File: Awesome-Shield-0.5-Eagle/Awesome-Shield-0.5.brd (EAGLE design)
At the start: 100 x 80 mm, 24 parts, among them J1 ARDUINO_R3_SHIELDUNO_R3_SHIEL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, SW1 SPST_TACT-EVQQ2

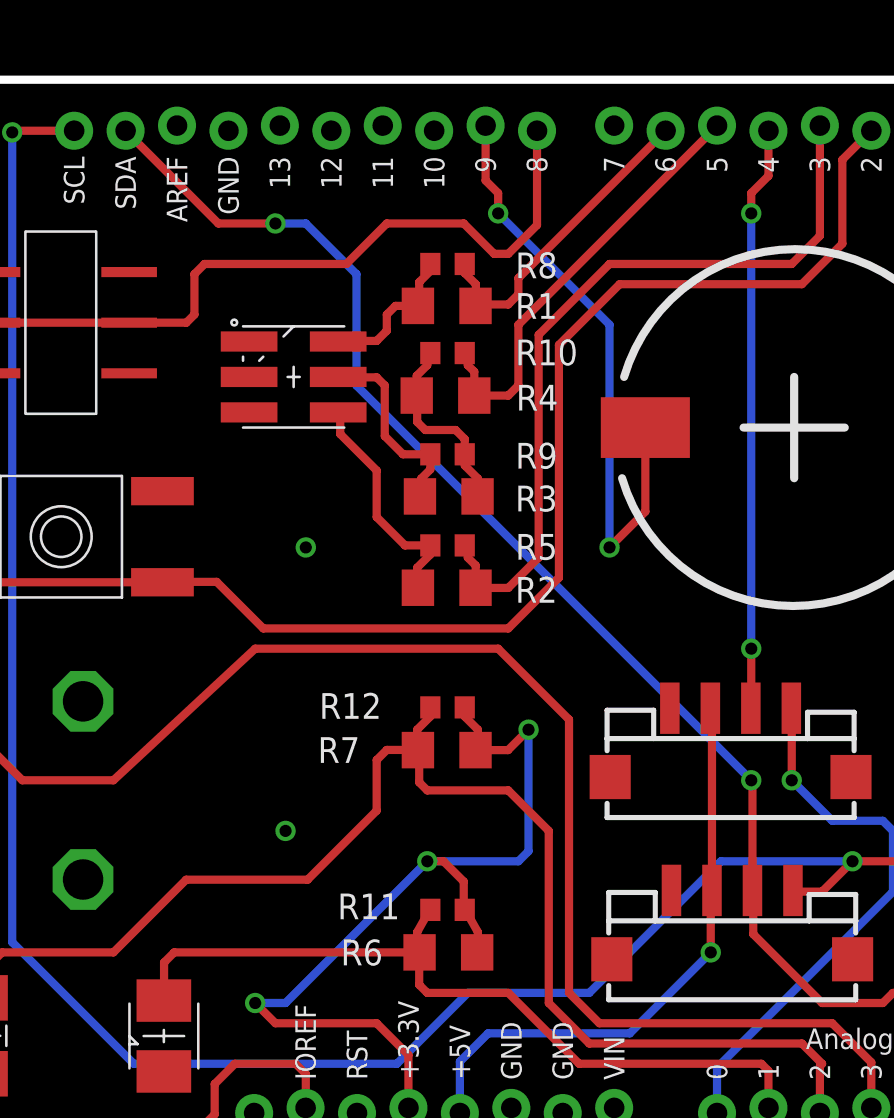
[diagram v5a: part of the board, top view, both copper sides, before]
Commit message: removed redundant vias, trace tweaks
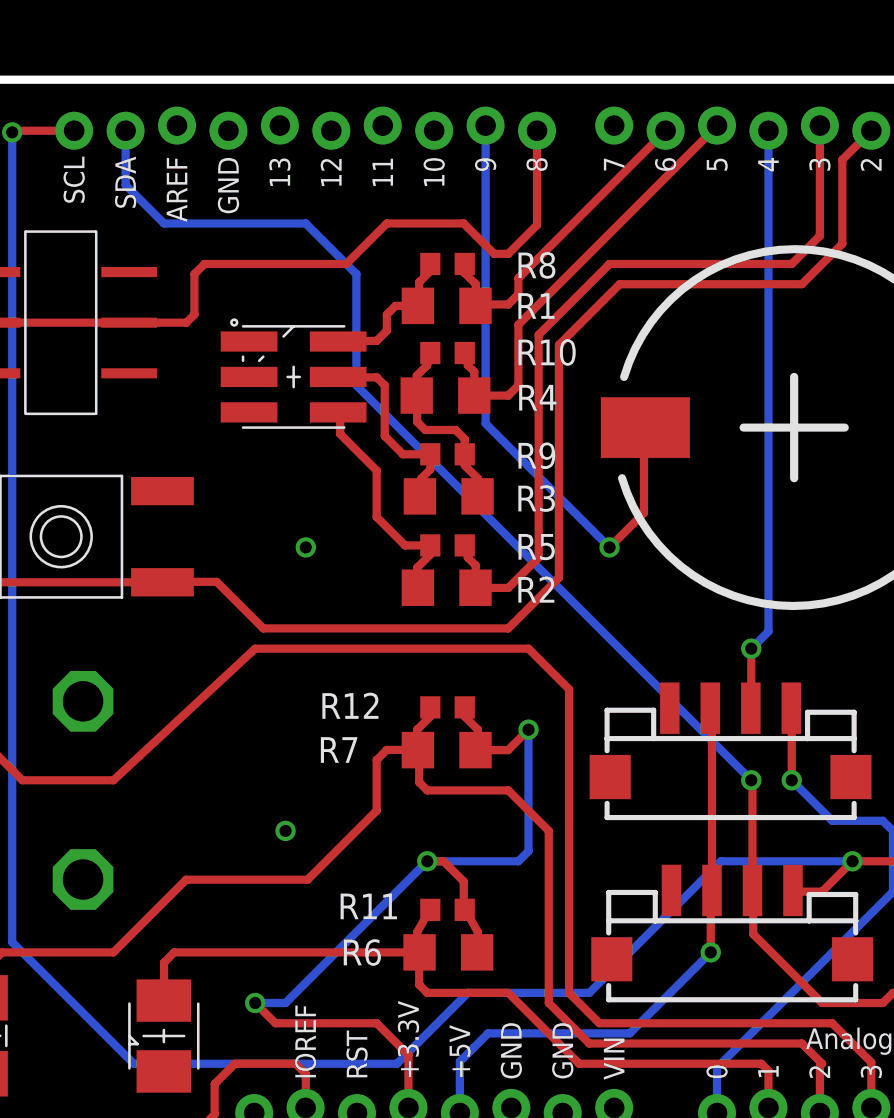
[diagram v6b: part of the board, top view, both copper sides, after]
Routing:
- net SDA: track 65.1 -> 66.6 mm, vias 2 -> 1
- net A3: track 67.9 -> 68.8 mm
- net D9: vias 2 -> 1
- net D4: vias 2 -> 1
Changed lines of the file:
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@@
 <contactref element="J5" pad="1"/>
 <contactref element="SJ2" pad="1"/>
-<wire x1="35.56" y1="68.58" x2="32.58" y2="68.58" width="0.4064" layer="1"/>
 <wire x1="32.58" y1="68.58" x2="32.5" y2="68.5" width="0.4064" layer="1"/>
 <via x="32.5" y="68.5" extent="1-16" drill="0.6"/>
@@
 <wire x1="51.5" y1="22.5" x2="55" y2="26" width="0.4064" layer="16"/>
 <wire x1="55" y1="26" x2="61" y2="26" width="0.4064" layer="16"/>
+<wire x1="35.56" y1="68.58" x2="32.58" y2="68.58" width="0.4064" layer="1"/>
 </signal>
 <signal name="SDA">
@@
 <wire x1="69" y1="36.5" x2="49.5" y2="56" width="0.4064" layer="16"/>
 <wire x1="49.5" y1="56" x2="49.5" y2="61.5" width="0.4064" layer="16"/>
-<via x="45.5" y="64" extent="1-16" drill="0.6"/>
-<wire x1="45.5" y1="64" x2="42.68" y2="64" width="0.4064" layer="1"/>
-<wire x1="42.68" y1="64" x2="38.1" y2="68.58" width="0.4064" layer="1"/>
 <wire x1="72.5" y1="25.5" x2="75.5" y2="25.5" width="0.4064" layer="1"/>
 <wire x1="75.5" y1="25.5" x2="76" y2="26" width="0.4064" layer="1"/>
@@
 <wire x1="77.492" y1="26" x2="77.5" y2="26.008" width="0.4064" layer="1"/>
 <wire x1="49.5" y1="61.5" x2="47" y2="64" width="0.4064" layer="16"/>
-<wire x1="47" y1="64" x2="45.5" y2="64" width="0.4064" layer="16"/>
+<wire x1="38.1" y1="68.58" x2="38.1" y2="65.9" width="0.4064" layer="16"/>
+<wire x1="38.1" y1="65.9" x2="40" y2="64" width="0.4064" layer="16"/>
+<wire x1="40" y1="64" x2="47" y2="64" width="0.4064" layer="16"/>
 </signal>
 <signal name="D8">
@@
 <contactref element="J1" pad="D9"/>
 <contactref element="SG1" pad="-"/>
-<wire x1="63.77" y1="53.92" x2="63.77" y2="49.77" width="0.4064" layer="1"/>
-<wire x1="63.77" y1="49.77" x2="62" y2="48" width="0.4064" layer="1"/>
+<wire x1="55.88" y1="68.834" x2="55.88" y2="54.12" width="0.4064" layer="16"/>
+<wire x1="55.88" y1="54.12" x2="62" y2="48" width="0.4064" layer="16"/>
 <via x="62" y="48" extent="1-16" drill="0.6"/>
-<wire x1="62" y1="48" x2="62" y2="59" width="0.4064" layer="16"/>
-<wire x1="62" y1="59" x2="56.5" y2="64.5" width="0.4064" layer="16"/>
-<via x="56.5" y="64.5" extent="1-16" drill="0.6"/>
-<wire x1="56.5" y1="64.5" x2="56.5" y2="65.5" width="0.4064" layer="1"/>
-<wire x1="55.88" y1="68.834" x2="55.88" y2="66.12" width="0.4064" layer="1"/>
-<wire x1="55.88" y1="66.12" x2="56.5" y2="65.5" width="0.4064" layer="1"/>
+<wire x1="62" y1="48" x2="63.7" y2="49.7" width="0.4064" layer="1"/>
+<wire x1="63.7" y1="49.7" x2="63.7" y2="53.85" width="0.4064" layer="1"/>
+<wire x1="63.7" y1="53.85" x2="63.77" y2="53.92" width="0.4064" layer="1"/>
 </signal>
 <signal name="D4">
 <contactref element="J1" pad="D4"/>
 <contactref element="J2" pad="2"/>
-<wire x1="69.85" y1="68.58" x2="69.85" y2="66.35" width="0.4064" layer="1"/>
-<via x="69" y="64.5" extent="1-16" drill="0.6"/>
-<wire x1="69" y1="64.5" x2="69" y2="43" width="0.4064" layer="16"/>
 <via x="69" y="43" extent="1-16" drill="0.6"/>
 <wire x1="69" y1="43" x2="69" y2="40.08" width="0.4064" layer="1"/>
 <wire x1="69" y1="40.08" x2="68.98" y2="40.06" width="0.4064" layer="1"/>
-<wire x1="69.85" y1="66.35" x2="69" y2="65.5" width="0.4064" layer="1"/>
-<wire x1="69" y1="65.5" x2="69" y2="64.5" width="0.4064" layer="1"/>
+<wire x1="69.85" y1="68.58" x2="69.85" y2="43.85" width="0.4064" layer="16"/>
+<wire x1="69.85" y1="43.85" x2="69" y2="43" width="0.4064" layer="16"/>
 </signal>
 <signal name="N$2">
@@
 <wire x1="74.93" y1="22.57" x2="73" y2="24.5" width="0.4064" layer="1"/>
 <wire x1="73" y1="24.5" x2="61.5" y2="24.5" width="0.4064" layer="1"/>
-<wire x1="60" y1="39.5" x2="56.5" y2="43" width="0.4064" layer="1"/>
-<wire x1="56.5" y1="43" x2="44.5" y2="43" width="0.4064" layer="1"/>
+<wire x1="58" y1="43" x2="44.5" y2="43" width="0.4064" layer="1"/>
 <wire x1="44.5" y1="43" x2="37.5" y2="36.5" width="0.4064" layer="1"/>
 <wire x1="37.5" y1="36.5" x2="33" y2="36.5" width="0.4064" layer="1"/>
@@
 <wire x1="31" y1="38.5" x2="29" y2="38.5" width="0.4064" layer="1"/>
 <wire x1="61.5" y1="24.5" x2="60" y2="26" width="0.4064" layer="1"/>
-<wire x1="60" y1="26" x2="60" y2="39.5" width="0.4064" layer="1"/>
+<wire x1="60" y1="26" x2="60" y2="41" width="0.4064" layer="1"/>
+<wire x1="58" y1="43" x2="60" y2="41" width="0.4064" layer="1"/>
 </signal>
 <signal name="IOREF">

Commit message: removed redundant via, trace nudges for GND pour coverage
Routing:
- net D3: track 38.4 -> 36.4 mm
- net SCL: track 103.5 -> 101.8 mm, vias 2 -> 1
- net D2: track 65.3 -> 64.2 mm
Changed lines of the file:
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@@
 <via x="46" y="34" extent="1-16" drill="0.6"/>
 <via x="81" y="45.5" extent="1-16" drill="0.6"/>
+<via x="30" y="66" extent="1-16" drill="0.6"/>
 <wire x1="74.006" y1="27.66" x2="73.926" y2="36.66" width="0" layer="19" extent="1-1"/>
 </signal>
@@
 <wire x1="57" y1="44" x2="59.5" y2="46.5" width="0.4064" layer="1"/>
 <wire x1="59.5" y1="46.5" x2="59.5" y2="58" width="0.4064" layer="1"/>
-<wire x1="59.5" y1="58" x2="62.5" y2="61" width="0.4064" layer="1"/>
-<wire x1="62.5" y1="61" x2="71.5" y2="61" width="0.4064" layer="1"/>
-<wire x1="71.5" y1="61" x2="73.5" y2="63" width="0.4064" layer="1"/>
-<wire x1="73.5" y1="63" x2="73.5" y2="67.15" width="0.4064" layer="1"/>
-<wire x1="73.5" y1="67.15" x2="74.93" y2="68.58" width="0.4064" layer="1"/>
 <wire x1="44.9" y1="44" x2="42.6" y2="46.3" width="0.4064" layer="1"/>
 <wire x1="42.6" y1="46.3" x2="39.94" y2="46.3" width="0.4064" layer="1"/>
 <wire x1="39.94" y1="46.3" x2="39.92" y2="46.28" width="0.4064" layer="1"/>
+<wire x1="59.5" y1="58" x2="67" y2="65.5" width="0.4064" layer="1"/>
+<wire x1="67" y1="65.5" x2="74" y2="65.5" width="0.4064" layer="1"/>
+<wire x1="74" y1="65.5" x2="75" y2="66.5" width="0.4064" layer="1"/>
+<wire x1="75" y1="66.5" x2="75" y2="68.51" width="0.4064" layer="1"/>
+<wire x1="75" y1="68.51" x2="74.93" y2="68.58" width="0.4064" layer="1"/>
 </signal>
 <signal name="D6">
@@
 <contactref element="J5" pad="1"/>
 <contactref element="SJ2" pad="1"/>
-<wire x1="32.58" y1="68.58" x2="32.5" y2="68.5" width="0.4064" layer="1"/>
-<via x="32.5" y="68.5" extent="1-16" drill="0.6"/>
-<wire x1="32.5" y1="68.5" x2="32.5" y2="28.5" width="0.4064" layer="16"/>
 <via x="74" y="32.5" extent="1-16" drill="0.6"/>
 <wire x1="71" y1="31.12" x2="71.06" y2="31.06" width="0.4064" layer="1"/>
@@
 <wire x1="71.12" y1="31" x2="71.06" y2="31.06" width="0.4064" layer="1"/>
 <wire x1="67.5" y1="32.5" x2="61" y2="26" width="0.4064" layer="16"/>
-<wire x1="38.5" y1="22.5" x2="32.5" y2="28.5" width="0.4064" layer="16"/>
+<wire x1="38.5" y1="22.5" x2="33" y2="28" width="0.4064" layer="16"/>
 <wire x1="74" y1="32.5" x2="67.5" y2="32.5" width="0.4064" layer="16"/>
 <wire x1="38.5" y1="22.5" x2="51.5" y2="22.5" width="0.4064" layer="16"/>
 <wire x1="51.5" y1="22.5" x2="55" y2="26" width="0.4064" layer="16"/>
 <wire x1="55" y1="26" x2="61" y2="26" width="0.4064" layer="16"/>
-<wire x1="35.56" y1="68.58" x2="32.58" y2="68.58" width="0.4064" layer="1"/>
+<wire x1="35.56" y1="68.58" x2="35.56" y2="68.56" width="0.4064" layer="16"/>
+<wire x1="35.56" y1="68.56" x2="32.5" y2="65.5" width="0.4064" layer="16"/>
+<wire x1="32.5" y1="65.5" x2="32.5" y2="28.5" width="0.4064" layer="16"/>
+<wire x1="32.5" y1="28.5" x2="33" y2="28" width="0.4064" layer="16"/>
 </signal>
 <signal name="SDA">
@@
 <contactref element="R5" pad="1"/>
 <contactref element="R2" pad="1"/>
-<wire x1="72.39" y1="68.834" x2="72.39" y2="63.39" width="0.4064" layer="1"/>
 <wire x1="55.392" y1="46" x2="55.392" y2="47.108" width="0.4064" layer="1"/>
 <wire x1="55.392" y1="47.108" x2="55" y2="47.5" width="0.4064" layer="1"/>
 <wire x1="55" y1="47.5" x2="55" y2="47.85" width="0.4064" layer="1"/>
 <wire x1="55" y1="47.85" x2="54.85" y2="48.1" width="0.4064" layer="1"/>
-<wire x1="72.39" y1="63.39" x2="71" y2="62" width="0.4064" layer="1"/>
-<wire x1="71" y1="62" x2="62" y2="62" width="0.4064" layer="1"/>
-<wire x1="62" y1="62" x2="58.5" y2="58.5" width="0.4064" layer="1"/>
 <wire x1="58.5" y1="58.5" x2="58.5" y2="47.5" width="0.4064" layer="1"/>
 <wire x1="58.5" y1="47.5" x2="57" y2="46" width="0.4064" layer="1"/>
 <wire x1="57" y1="46" x2="55.392" y2="46" width="0.4064" layer="1"/>
 <wire x1="55.392" y1="46" x2="55.382" y2="46.01" width="0.4064" layer="1"/>
+<wire x1="58.5" y1="58.5" x2="66.5" y2="66.5" width="0.4064" layer="1"/>
+<wire x1="66.5" y1="66.5" x2="72" y2="66.5" width="0.4064" layer="1"/>
+<wire x1="72" y1="66.5" x2="72.5" y2="67" width="0.4064" layer="1"/>
+<wire x1="72.5" y1="67" x2="72.5" y2="68.724" width="0.4064" layer="1"/>
+<wire x1="72.5" y1="68.724" x2="72.39" y2="68.834" width="0.4064" layer="1"/>
 </signal>
 <signal name="N$9">

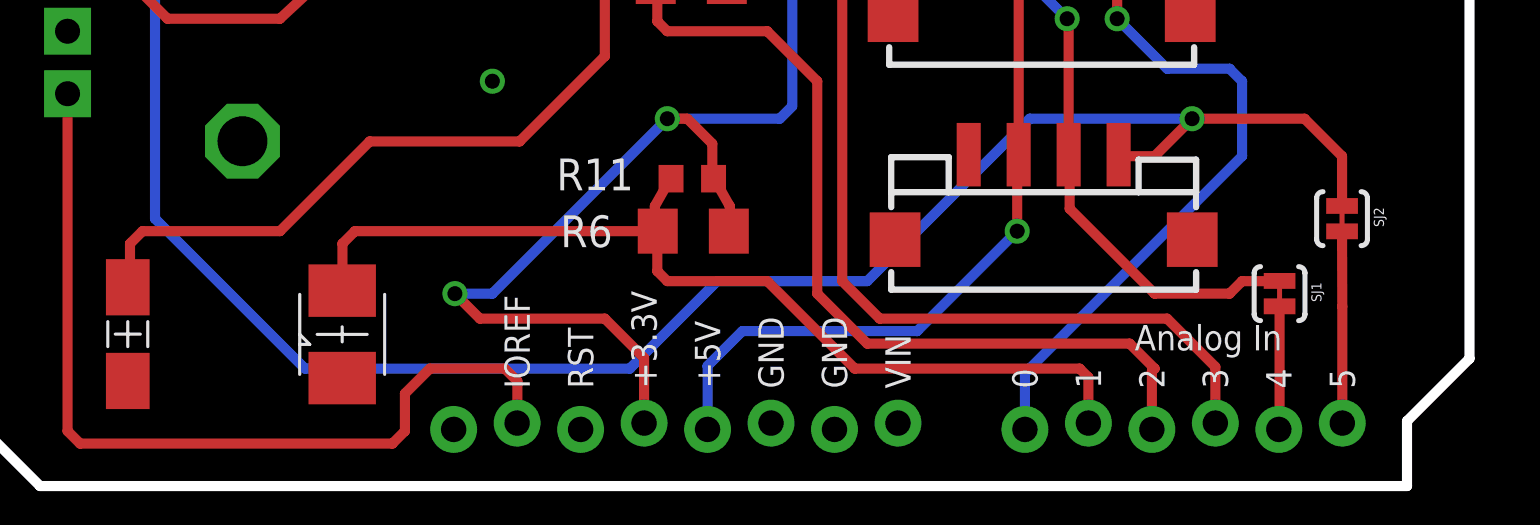
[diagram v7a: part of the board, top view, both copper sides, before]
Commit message: alligned solder bridge pads to make cutting them easier
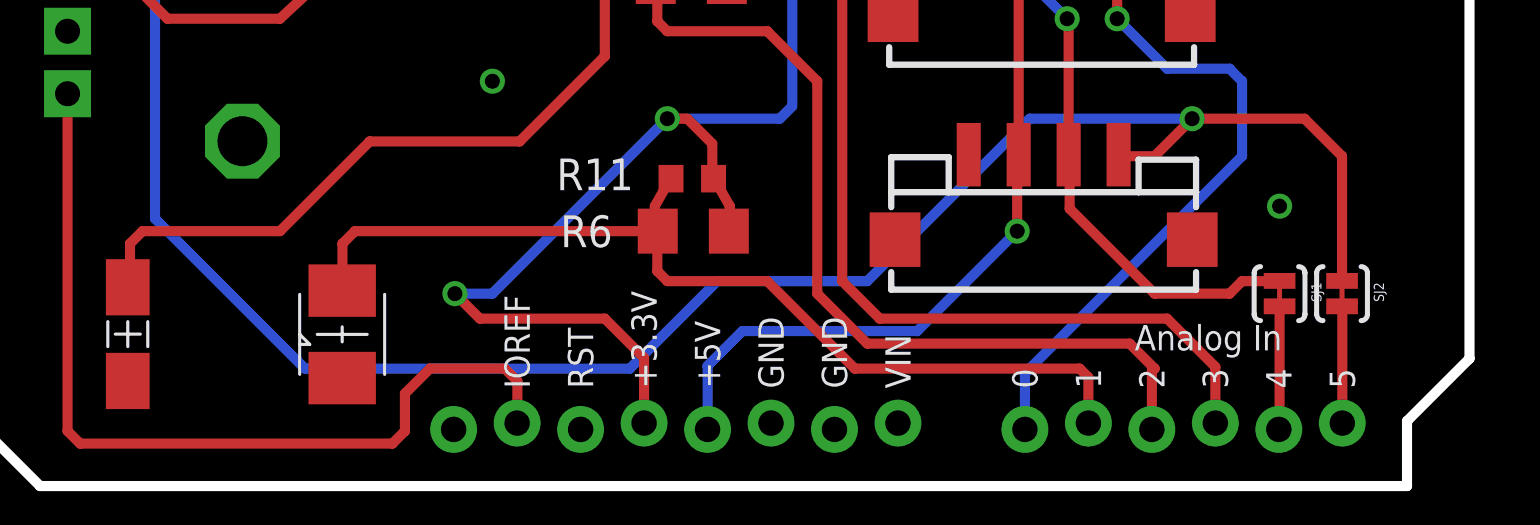
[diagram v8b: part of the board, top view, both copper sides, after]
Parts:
- moved SJ2 3.00 mm to (80.0, 25.5)
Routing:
- net SCL: track 101.8 -> 104.8 mm
- net A5: track 7.67 -> 4.68 mm
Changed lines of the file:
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@@
 <attribute name="NAME" x="78.77" y="25.9525" size="0.4064" layer="25" rot="R270"/>
 </element>
-<element name="SJ2" library="SparkFun-Passives" package="PAD-JUMPER-2-NC_BY_TRACE_YES_SILK" value="JUMPER-PAD-2-NC_BY_TRACE" x="80" y="28.5" smashed="yes" rot="R270">
-<attribute name="NAME" x="81.27" y="28.9525" size="0.4064" layer="25" rot="R270"/>
+<element name="SJ2" library="SparkFun-Passives" package="PAD-JUMPER-2-NC_BY_TRACE_YES_SILK" value="JUMPER-PAD-2-NC_BY_TRACE" x="80" y="25.5" smashed="yes" rot="R270">
+<attribute name="NAME" x="81.27" y="25.9525" size="0.4064" layer="25" rot="R270"/>
 </element>
 <element name="S2" library="SparkFun-Electromechanical" package="AYZ0202" value="DPDT" x="34.9" y="59.1" smashed="yes" rot="R270">
@@
 <via x="81" y="45.5" extent="1-16" drill="0.6"/>
 <via x="30" y="66" extent="1-16" drill="0.6"/>
-<wire x1="74.006" y1="27.66" x2="73.926" y2="36.66" width="0" layer="19" extent="1-1"/>
+<via x="77.5" y="29" extent="1-16" drill="0.6"/>
 </signal>
 <signal name="A2">
@@
 <contactref element="SJ2" pad="2"/>
 <wire x1="80.01" y1="20.32" x2="80.01" y2="24.982" width="0.4064" layer="1"/>
-<wire x1="80.01" y1="24.982" x2="80" y2="27.992" width="0.4064" layer="1"/>
+<wire x1="80.01" y1="24.982" x2="80" y2="24.992" width="0.4064" layer="1"/>
 </signal>
 <signal name="A4">
@@
 <via x="74" y="32.5" extent="1-16" drill="0.6"/>
 <wire x1="71" y1="31.12" x2="71.06" y2="31.06" width="0.4064" layer="1"/>
-<wire x1="80" y1="29.008" x2="80" y2="31" width="0.4064" layer="1"/>
+<wire x1="80" y1="26.008" x2="80" y2="31" width="0.4064" layer="1"/>
 <wire x1="80" y1="31" x2="78.5" y2="32.5" width="0.4064" layer="1"/>
 <wire x1="78.5" y1="32.5" x2="74" y2="32.5" width="0.4064" layer="1"/>
@@
 <wire x1="71.12" y1="31" x2="71.06" y2="31.06" width="0.4064" layer="1"/>
 <wire x1="67.5" y1="32.5" x2="61" y2="26" width="0.4064" layer="16"/>
-<wire x1="38.5" y1="22.5" x2="33" y2="28" width="0.4064" layer="16"/>
+<wire x1="38.5" y1="22.5" x2="32.5" y2="28.5" width="0.4064" layer="16"/>
 <wire x1="74" y1="32.5" x2="67.5" y2="32.5" width="0.4064" layer="16"/>
 <wire x1="38.5" y1="22.5" x2="51.5" y2="22.5" width="0.4064" layer="16"/>
@@
 <wire x1="35.56" y1="68.56" x2="32.5" y2="65.5" width="0.4064" layer="16"/>
 <wire x1="32.5" y1="65.5" x2="32.5" y2="28.5" width="0.4064" layer="16"/>
-<wire x1="32.5" y1="28.5" x2="33" y2="28" width="0.4064" layer="16"/>
 </signal>
 <signal name="SDA">
